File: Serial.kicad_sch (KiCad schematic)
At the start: 4 parts, among them J3 D09P33E4GX00LF

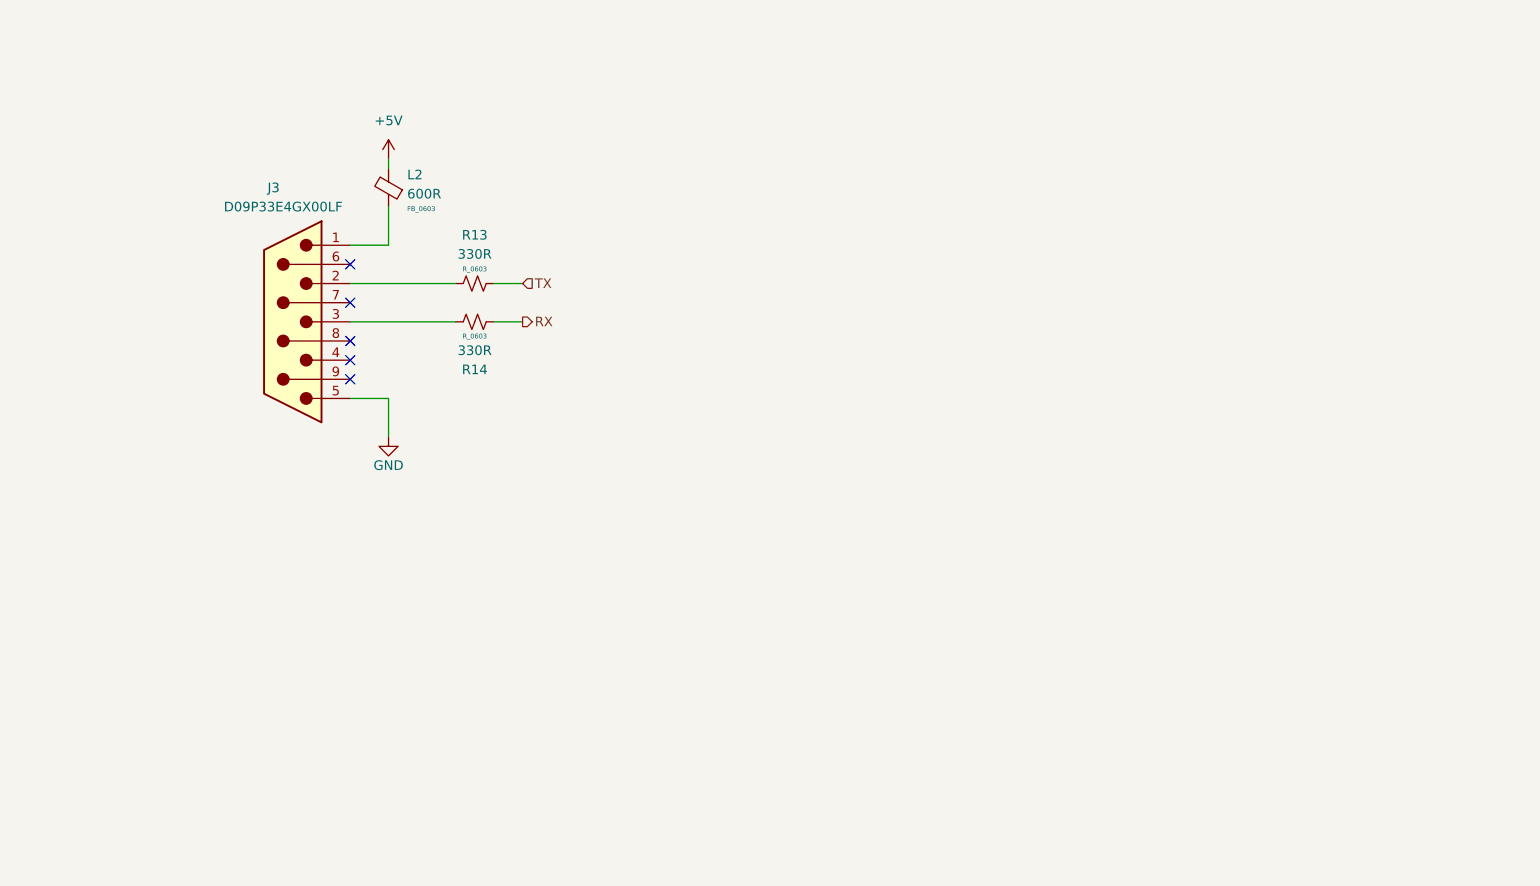
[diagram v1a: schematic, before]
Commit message: Add in RS232
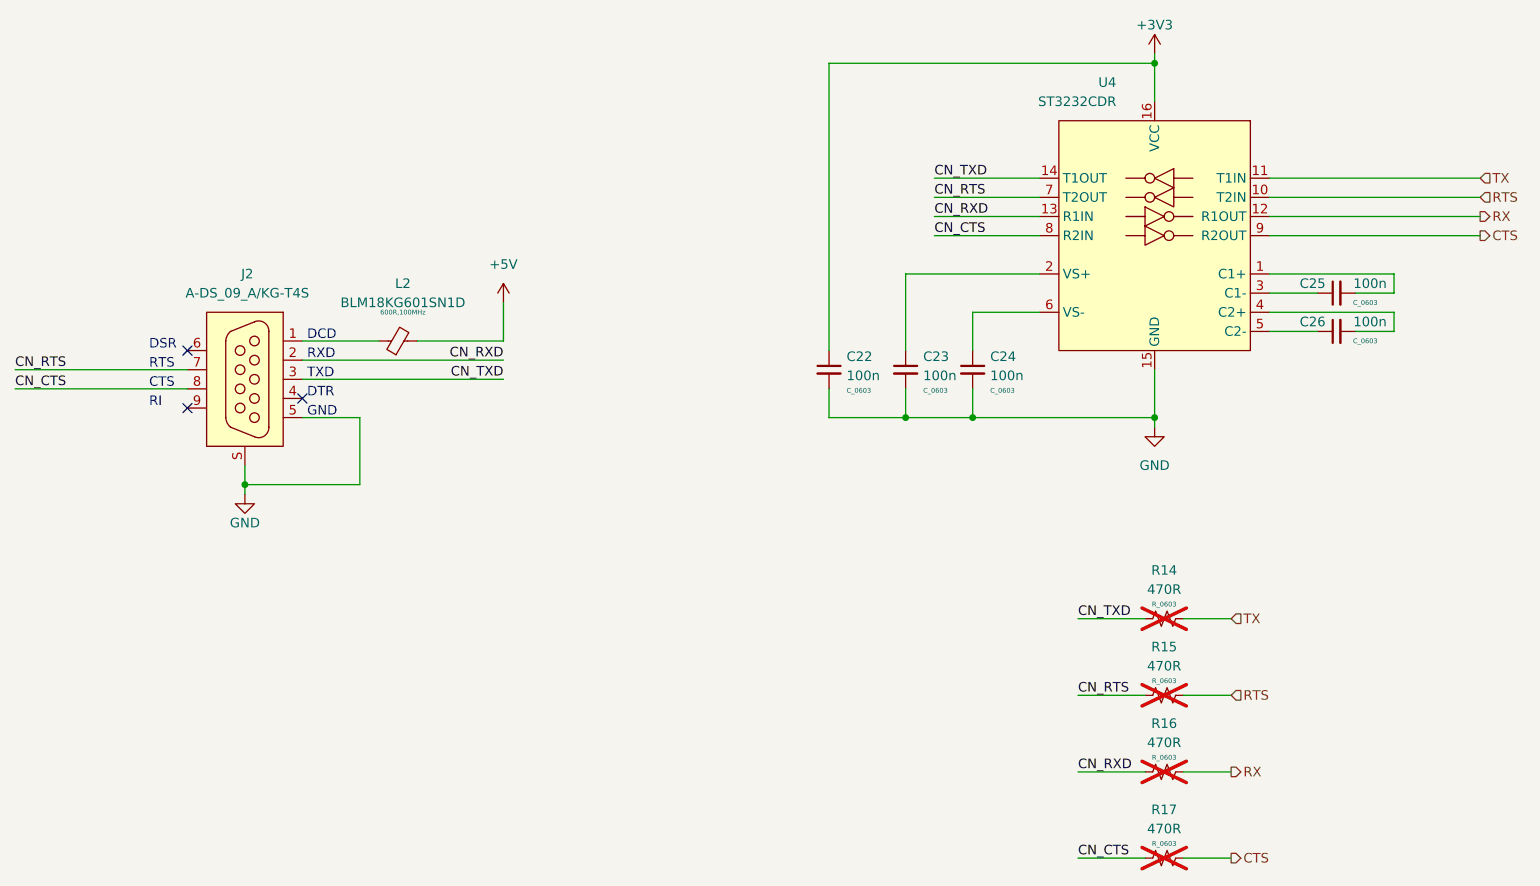
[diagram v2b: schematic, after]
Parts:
- removed J3: D09P33E4GX00LF, Connector_Dsub:DSUB-9_Male_Horizontal_P2.77x2.84mm_EdgePinOffset7.70mm_Housed_MountingHolesOffset9.12mm, symbol Connector:DB9_Male
- removed L2: 600R, L_Inductor:FB_0603, symbol L_Inductor:FB_0603
- removed R13: 330R, R_Resistor:R_0603, symbol R_Resistor:R_0603
- added C22, C23, C24, C25, C26: 100n, C_Capacitor:C_0603, symbol C_Capacitor:C_0603
- added J2: A-DS_09_A/KG-T4S, J_Connector:DSUB09_Male_Horizontal, symbol J_Connector:A-DS_09_A/KG-T4S
- added L2: BLM18KG601SN1D, L_Inductor:FB_0603, symbol L_Inductor:BLM18KG601SN1D
- added R15, R16, R17: 470R, R_Resistor:R_0603, symbol R_Resistor:R_0603
- added U4: ST3232CDR, U_IC:SOIC_16, symbol U_Transceiver:ST3232CDR
- R14: value 330R -> 470R; now not fitted
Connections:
- net +5V: now also L2.2
- net GND: now also C22.2, C23.2, C24.2, J2.5, J2.S, U4.15 (GND)
- net RX: now also R16.2, U4.12 (R1OUT); no longer R14.2
- net TX: now also R14.2, U4.11 (T1IN)
- net CN_TXD: now reaches R14.1
- net CN_TXD: now also J2.3, U4.14 (T1OUT)
- new net: C24.1, U4.6 (VS-)
- new net: C25.1, U4.3 (C1-)
- new net: C25.2, U4.1 (C1+)
- new net: J2.1, L2.1
- new net: C23.1, U4.2 (VS+)
- new net: C26.2, U4.4 (C2+)
- new net: C26.1, U4.5 (C2-)
- new net +3V3: C22.1, U4.16 (VCC)
- new net CN_CTS: J2.8, R17.1, U4.8 (R2IN)
- new net CN_RTS: J2.7, R15.1, U4.7 (T2OUT)
- new net CN_RXD: J2.2, R16.1, U4.13 (R1IN)
- new net CTS: R17.2, U4.9 (R2OUT)
- new net RTS: R15.2, U4.10 (T2IN)
- no-connect marks 5 -> 3
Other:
- note added: "CTS"
- note added: "DCD"
- note added: "DSR"
- note added: "DTR"
- note added: "GND"
- note added: "RI"
- note added: "RTS"
- note added: "RXD"
- note added: "TXD"
- company: TL Embedded Ltd -> TL Embedded

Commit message: PCB Layout
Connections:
- net CN_CTS: now also U4.13 (R1IN); no longer U4.8 (R2IN)
- net CN_RTS: now also U4.14 (T1OUT); no longer U4.7 (T2OUT)
- net CN_RXD: now also U4.8 (R2IN); no longer U4.13 (R1IN)
- net CN_TXD: now also U4.7 (T2OUT); no longer U4.14 (T1OUT)
- net CTS: now also U4.12 (R1OUT); no longer U4.9 (R2OUT)
- net RTS: now also U4.11 (T1IN); no longer U4.10 (T2IN)
- net RX: now also U4.9 (R2OUT); no longer U4.12 (R1OUT)
- net TX: now also U4.10 (T2IN); no longer U4.11 (T1IN)
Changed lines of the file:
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@@
 	(title_block
 		(title "Serial-Ethernet")
-		(date "2026-07-23")
+		(date "2026-07-25")
 		(rev "v1.1")
 		(company "TL Embedded")
@@
 	(wire
 		(pts
-			(xy 162.56 66.04) (xy 176.53 66.04)
+			(xy 158.75 66.04) (xy 176.53 66.04)
 		)
 		(stroke
@@
 	(wire
 		(pts
-			(xy 207.01 60.96) (xy 234.95 60.96)
+			(xy 207.01 60.96) (xy 223.52 60.96)
 		)
 		(stroke
@@
 	(wire
 		(pts
-			(xy 207.01 66.04) (xy 234.95 66.04)
+			(xy 207.01 66.04) (xy 223.52 66.04)
 		)
 		(stroke
@@
 	(wire
 		(pts
-			(xy 162.56 63.5) (xy 176.53 63.5)
-		)
-		(stroke
-			(width 0)
-			(type default)
-		)
-	)
-	(wire
-		(pts
-			(xy 207.01 58.42) (xy 234.95 58.42)
+			(xy 158.75 63.5) (xy 176.53 63.5)
+		)
+		(stroke
+			(width 0)
+			(type default)
+		)
+	)
+	(wire
+		(pts
+			(xy 207.01 58.42) (xy 223.52 58.42)
 		)
 		(stroke
@@
 	(wire
 		(pts
-			(xy 162.56 58.42) (xy 176.53 58.42)
+			(xy 158.75 58.42) (xy 176.53 58.42)
 		)
 		(stroke
@@
 	(wire
 		(pts
-			(xy 207.01 63.5) (xy 234.95 63.5)
+			(xy 207.01 63.5) (xy 223.52 63.5)
 		)
 		(stroke
@@
 	(wire
 		(pts
-			(xy 162.56 60.96) (xy 176.53 60.96)
+			(xy 158.75 60.96) (xy 176.53 60.96)
 		)
 		(stroke
@@
 			(width 0)
 			(type default)
-		)
-	)
-	(label "CN_CTS"
-		(at 162.56 66.04 0)
-		(effects
-			(font
-				(size 1.27 1.27)
-			)
-			(justify left bottom)
-		)
-	)
-	(label "CN_RXD"
-		(at 162.56 63.5 0)
-		(effects
-			(font
-				(size 1.27 1.27)
-			)
-			(justify left bottom)
 		)
 	)
@@
 		)
 	)
+	(label "CN_CTS"
+		(at 158.75 63.5 0)
+		(effects
+			(font
+				(size 1.27 1.27)
+			)
+			(justify left bottom)
+		)
+	)
 	(label "CN_TXD"
 		(at 105.41 85.09 180)
@@
 		)
 	)
+	(label "CN_TXD"
+		(at 158.75 60.96 0)
+		(effects
+			(font
+				(size 1.27 1.27)
+			)
+			(justify left bottom)
+		)
+	)
+	(label "CN_RTS"
+		(at 158.75 58.42 0)
+		(effects
+			(font
+				(size 1.27 1.27)
+			)
+			(justify left bottom)
+		)
+	)
 	(label "CN_RXD"
 		(at 181.61 137.16 0)
@@
 		)
 	)
-	(label "CN_TXD"
-		(at 162.56 58.42 0)
-		(effects
-			(font
-				(size 1.27 1.27)
-			)
-			(justify left bottom)
-		)
-	)
-	(label "CN_RTS"
-		(at 162.56 60.96 0)
+	(label "CN_RXD"
+		(at 158.75 66.04 0)
 		(effects
 			(font
@@
 		)
 	)
+	(hierarchical_label "RX"
+		(shape output)
+		(at 223.52 66.04 0)
+		(effects
+			(font
+				(size 1.27 1.27)
+			)
+			(justify left)
+		)
+	)
 	(hierarchical_label "RTS"
 		(shape input)
@@
 		)
 	)
-	(hierarchical_label "CTS"
-		(shape output)
-		(at 234.95 66.04 0)
-		(effects
-			(font
-				(size 1.27 1.27)
-			)
-			(justify left)
-		)
-	)
-	(hierarchical_label "RTS"
-		(shape input)
-		(at 234.95 60.96 0)
-		(effects
-			(font
-				(size 1.27 1.27)
-			)
-			(justify left)
-		)
-	)
 	(hierarchical_label "RX"
 		(shape output)
@@
 		)
 	)
-	(hierarchical_label "RX"
+	(hierarchical_label "CTS"
 		(shape output)
-		(at 234.95 63.5 0)
+		(at 223.52 63.5 0)
+		(effects
+			(font
+				(size 1.27 1.27)
+			)
+			(justify left)
+		)
+	)
+	(hierarchical_label "RTS"
+		(shape input)
+		(at 223.52 58.42 0)
 		(effects
 			(font
@@
 	(hierarchical_label "TX"
 		(shape input)
-		(at 234.95 58.42 0)
-		(effects
-			(font
+		(at 223.52 60.96 0)
+		(effects
+			(font
